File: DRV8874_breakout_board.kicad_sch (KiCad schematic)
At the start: 11 parts, among them U2 DRV8874PWPR

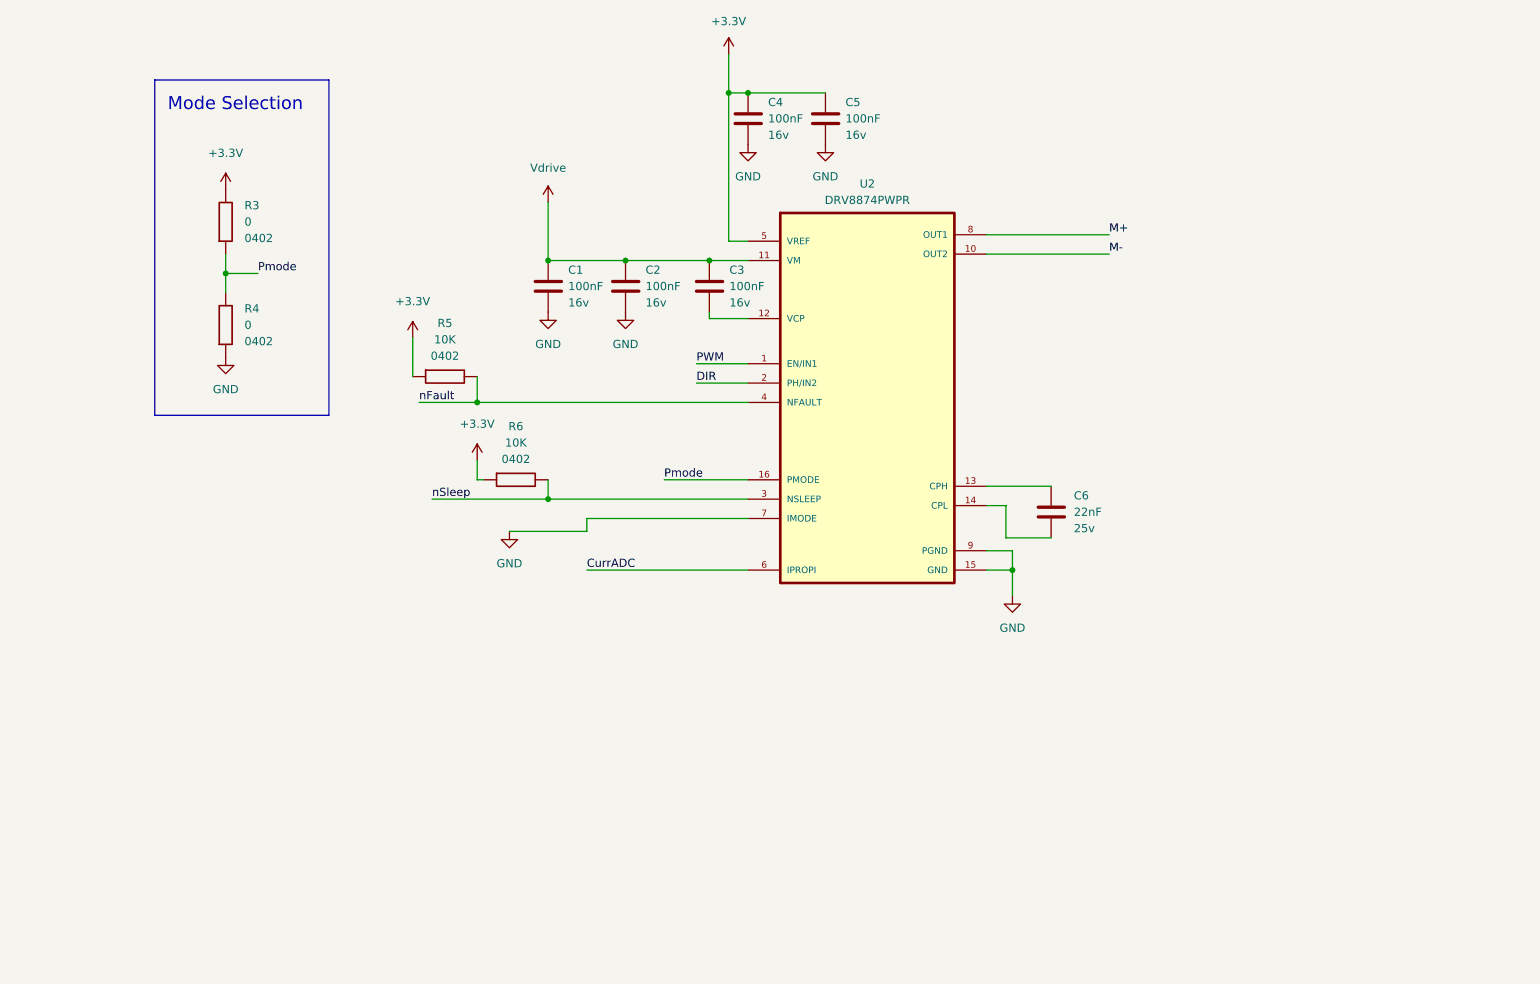
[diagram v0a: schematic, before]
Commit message: Forma de PCB con espacios para tira de pines
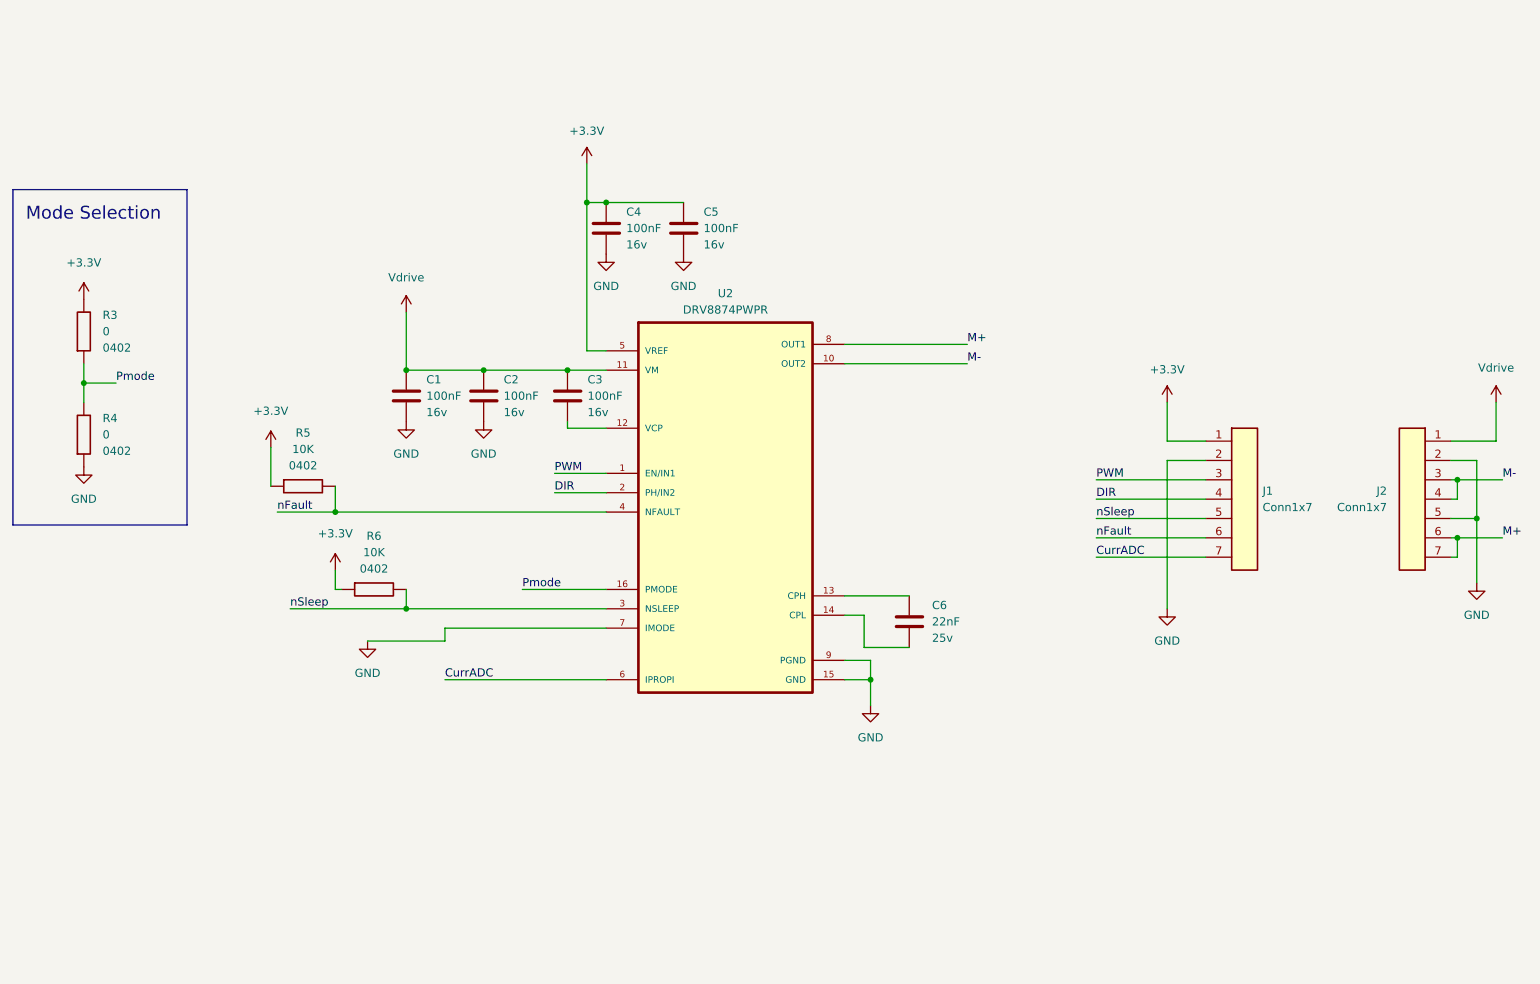
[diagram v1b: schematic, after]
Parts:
- added J1, J2: Conn1x7, Connector_PinHeader_2.54mm:PinHeader_1x07_P2.54mm_Vertical, symbol Herranz - Gen Connectors:Conn1x7
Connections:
- net +3V3: now also J1.1 (Pin_1)
- net CurrADC: now also J1.7 (Pin_7)
- net DIR: now also J1.4 (Pin_4)
- net GND: now also J1.2 (Pin_2), J2.2 (Pin_2), J2.5 (Pin_5)
- net M+: now also J2.6 (Pin_6), J2.7 (Pin_7)
- net M-: now also J2.3 (Pin_3), J2.4 (Pin_4)
- net PWM: now also J1.3 (Pin_3)
- net Vdrive: now also J2.1 (Pin_1)
- net nFault: now also J1.6 (Pin_6)
- net nSleep: now also J1.5 (Pin_5)
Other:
- moved on the sheet: C1, C2, C3, C4, C5, C6, R3, R4, R5, R6, U2

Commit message: primera iteración PCB
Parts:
- added R4: 0, Resistor_SMD:R_0402_1005Metric, symbol Herranz - Resistors (0402):0
- added R5: 62K, Resistor_SMD:R_0402_1005Metric, symbol Herranz - Resistors (0402):62K
- added U2: Logo_Small, Herranz - Various:LOGO_small, symbol Herranz - Various:Logo_Small
- R3: now not fitted
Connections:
- net CurrADC: now also R4.2
- net GND: now also R4.1, R5.1; no longer U2.7 (IMODE)
- new net: R5.2, U2.7 (IMODE)
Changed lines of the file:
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@@
   (junction (at 107 87) (diameter 0) (color 0 0 0 0)
   )
+  (junction (at 113 135) (diameter 0) (color 0 0 0 0)
+  )
   (junction (at 95 124) (diameter 0) (color 0 0 0 0)
   )
@@
     (stroke (width 0) (type default))
   )
+  (wire (pts (xy 84 129) (xy 84 127))
+    (stroke (width 0) (type default))
+  )
   (wire (pts (xy 264 98) (xy 264 92))
     (stroke (width 0) (type default))
@@
     (stroke (width 0) (type default))
   )
+  (wire (pts (xy 113 135) (xy 126 135))
+    (stroke (width 0) (type default))
+  )
   (wire (pts (xy 45 89) (xy 50 89))
     (stroke (width 0) (type default))
@@
     (stroke (width 0) (type default))
   )
-  (wire (pts (xy 89 129) (xy 101 129))
-    (stroke (width 0) (type default))
-  )
   (wire (pts (xy 257 113) (xy 258 113))
     (stroke (width 0) (type default))
@@
     (stroke (width 0) (type default))
   )
-  (wire (pts (xy 101 127) (xy 126 127))
+  (wire (pts (xy 84 127) (xy 126 127))
     (stroke (width 0) (type default))
   )
@@
     (stroke (width 0) (type default))
   )
-  (wire (pts (xy 101 135) (xy 126 135))
-    (stroke (width 0) (type default))
-  )
-  (wire (pts (xy 101 129) (xy 101 127))
+  (wire (pts (xy 101 135) (xy 113 135))
+    (stroke (width 0) (type default))
+  )
+  (wire (pts (xy 84 142) (xy 84 139))
     (stroke (width 0) (type default))
   )
@@
         (path "/a9814894-6caf-47c3-94af-538221f5e47e"
           (reference "#PWR04") (unit 1)
+        )
+      )
+    )
+  )
+  (symbol (lib_id "power:GND") (at 113 145 0) (unit 1)
+    (in_bom yes) (on_board yes) (dnp no) (fields_autoplaced)
+    (property "Reference" "#PWR0101" (at 113 151.35 0)
+      (effects (font (size 1.27 1.27)) hide)
+    )
+    (property "Value" "GND" (at 113 149.98 0)
+      (effects (font (size 1.27 1.27)))
+    )
+    (property "Footprint" "" (at 113 145 0)
+      (effects (font (size 1.27 1.27)) hide)
+    )
+    (property "Datasheet" "" (at 113 145 0)
+      (effects (font (size 1.27 1.27)) hide)
+    )
+    (pin "1")
+    (instances
+      (project "RosMechatronicBoard"
+        (path "/25a480f9-594a-4a75-8741-88ac7e0fd4ad/318900b3-2436-4284-bca8-0ffa65649c89"
+          (reference "#PWR0101") (unit 1)
+        )
+        (path "/25a480f9-594a-4a75-8741-88ac7e0fd4ad/8bbf1555-9781-4af3-bbc0-fdce319f9e3c"
+          (reference "#PWR010") (unit 1)
+        )
+        (path "/25a480f9-594a-4a75-8741-88ac7e0fd4ad/14e70d62-43dc-4725-9c42-40568e45ff10"
+          (reference "#PWR033") (unit 1)
+        )
+        (path "/25a480f9-594a-4a75-8741-88ac7e0fd4ad/d70baead-72f9-4a39-a1ce-4bdb0a4cab4d"
+          (reference "#PWR051") (unit 1)
+        )
+      )
+      (project "DRV8874_breakout_board"
+        (path "/a9814894-6caf-47c3-94af-538221f5e47e"
+          (reference "#PWR017") (unit 1)
         )
       )
@@
     )
   )
-  (symbol (lib_id "power:GND") (at 89 129 0) (unit 1)
-    (in_bom yes) (on_board yes) (dnp no) (fields_autoplaced)
-    (property "Reference" "#PWR0104" (at 89 135.35 0)
-      (effects (font (size 1.27 1.27)) hide)
-    )
-    (property "Value" "GND" (at 89 133.98 0)
-      (effects (font (size 1.27 1.27)))
-    )
-    (property "Footprint" "" (at 89 129 0)
-      (effects (font (size 1.27 1.27)) hide)
-    )
-    (property "Datasheet" "" (at 89 129 0)
+  (symbol (lib_id "power:GND") (at 84 142 0) (unit 1)
+    (in_bom yes) (on_board yes) (dnp no) (fields_autoplaced)
+    (property "Reference" "#PWR0104" (at 84 148.35 0)
+      (effects (font (size 1.27 1.27)) hide)
+    )
+    (property "Value" "GND" (at 84 146.98 0)
+      (effects (font (size 1.27 1.27)))
+    )
+    (property "Footprint" "" (at 84 142 0)
+      (effects (font (size 1.27 1.27)) hide)
+    )
+    (property "Datasheet" "" (at 84 142 0)
       (effects (font (size 1.27 1.27)) hide)
     )
@@
         (path "/a9814894-6caf-47c3-94af-538221f5e47e"
           (reference "C6") (unit 1)
+        )
+      )
+    )
+  )
+  (symbol (lib_id "Herranz - Various:Logo_Small") (at 188 178 0) (unit 1)
+    (in_bom yes) (on_board yes) (dnp no) (fields_autoplaced)
+    (property "Reference" "U2" (at 188 176 0)
+      (effects (font (size 1.27 1.27)) hide)
+    )
+    (property "Value" "Logo_Small" (at 188 181 0)
+      (effects (font (size 1.27 1.27)) hide)
+    )
+    (property "Footprint" "Herranz - Various:LOGO_small" (at 188 175 0)
+      (effects (font (size 1.27 1.27)) hide)
+    )
+    (property "Datasheet" "" (at 188 178 0)
+      (effects (font (size 1.27 1.27)) hide)
+    )
+    (instances
+      (project "DRV8874_breakout_board"
+        (path "/a9814894-6caf-47c3-94af-538221f5e47e"
+          (reference "U2") (unit 1)
         )
       )
@@
     )
   )
+  (symbol (lib_id "Herranz - Resistors (0402):62K") (at 83 134 90) (unit 1)
+    (in_bom yes) (on_board yes) (dnp no) (fields_autoplaced)
+    (property "Reference" "R5" (at 86.36 131.46 90)
+      (effects (font (size 1.27 1.27)) (justify right))
+    )
+    (property "Value" "62K" (at 86.36 134 90)
+      (effects (font (size 1.27 1.27)) (justify right))
+    )
+    (property "Footprint" "Resistor_SMD:R_0402_1005Metric" (at 80 134 0)
+      (effects (font (size 1.27 1.27)) hide)
+    )
+    (property "Datasheet" "" (at 83 134 0)
+      (effects (font (size 1.27 1.27)) hide)
+    )
+    (property "Size" "0402" (at 86.36 136.54 90)
+      (effects (font (size 1.27 1.27)) (justify right))
+    )
+    (pin "2")
+    (pin "1")
+    (instances
+      (project "DRV8874_breakout_board"
+        (path "/a9814894-6caf-47c3-94af-538221f5e47e"
+          (reference "R5") (unit 1)
+        )
+      )
+    )
+  )
   (symbol (lib_id "power:Vdrive") (at 95 78 0) (unit 1)
     (in_bom yes) (on_board yes) (dnp no) (fields_autoplaced)
@@
   )
   (symbol (lib_id "Herranz - Resistors (0402):0") (at 44 81 90) (unit 1)
-    (in_bom yes) (on_board yes) (dnp no) (fields_autoplaced)
+    (in_bom yes) (on_board yes) (dnp yes) (fields_autoplaced)
     (property "Reference" "R3" (at 47.91 78.46 90)
       (effects (font (size 1.27 1.27)) (justify right))
@@
         )
       )
+    )
+  )
+  (symbol (lib_id "Herranz - Resistors (0402):0") (at 112 140 90) (unit 1)
+    (in_bom yes) (on_board yes) (dnp no) (fields_autoplaced)
+    (property "Reference" "R4" (at 115.91 137.46 90)
+      (effects (font (size 1.27 1.27)) (justify right))
+    )
+    (property "Value" "0" (at 115.91 140 90)
+      (effects (font (size 1.27 1.27)) (justify right))
+    )
+    (property "Footprint" "Resistor_SMD:R_0402_1005Metric" (at 109 140 0)
+      (effects (font (size 1.27 1.27)) hide)
+    )
+    (property "Datasheet" "" (at 112 140 0)
+      (effects (font (size 1.27 1.27)) hide)
+    )
+    (property "Size" "0402" (at 115.91 142.54 90)
+      (effects (font (size 1.27 1.27)) (justify right))
+    )
+    (pin "1")
+    (pin "2")
+    (instances
+      (project "RosMechatronicBoard"
+        (path "/25a480f9-594a-4a75-8741-88ac7e0fd4ad/318900b3-2436-4284-bca8-0ffa65649c89"
+          (reference "R4") (unit 1)
+        )
+        (path "/25a480f9-594a-4a75-8741-88ac7e0fd4ad/8bbf1555-9781-4af3-bbc0-fdce319f9e3c"
+          (reference "R18") (unit 1)
+        )
+        (path "/25a480f9-594a-4a75-8741-88ac7e0fd4ad/14e70d62-43dc-4725-9c42-40568e45ff10"
+          (reference "R26") (unit 1)
+        )
+        (path "/25a480f9-594a-4a75-8741-88ac7e0fd4ad/d70baead-72f9-4a39-a1ce-4bdb0a4cab4d"
+          (reference "R34") (unit 1)
+        )
+      )
+      (project "DRV8874_breakout_board"
+        (path "/a9814894-6caf-47c3-94af-538221f5e47e"
+          (reference "R6") (unit 1)
+        )
+      )

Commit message: Añadido divisor de resistencia para v_ref
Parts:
- removed C4, C5: 100nF, Capacitor_SMD:C_0603_1608Metric, symbol Herranz - Capacitor (0603):Gen_C
- added C3: Gen_C, Capacitor_SMD:C_0402_1005Metric, symbol Herranz - Capacitor (0402):Gen_C
- added R6, R7: 0, Resistor_SMD:R_0402_1005Metric, symbol Herranz - Resistors (0402):0
- renumbered C1 to C?, C6 to C?, C2 to C?, C3 to C?, R5 to R4, R5 to R?, R6 to R?, R4 to R?, R3 to R?, U2 to U?
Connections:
- net +3V3: now also R6.2; no longer U?.5 (VREF)
- net GND: now also C3.2, R7.1
- new net: C3.1, R6.1, R7.2, U?.5 (VREF)

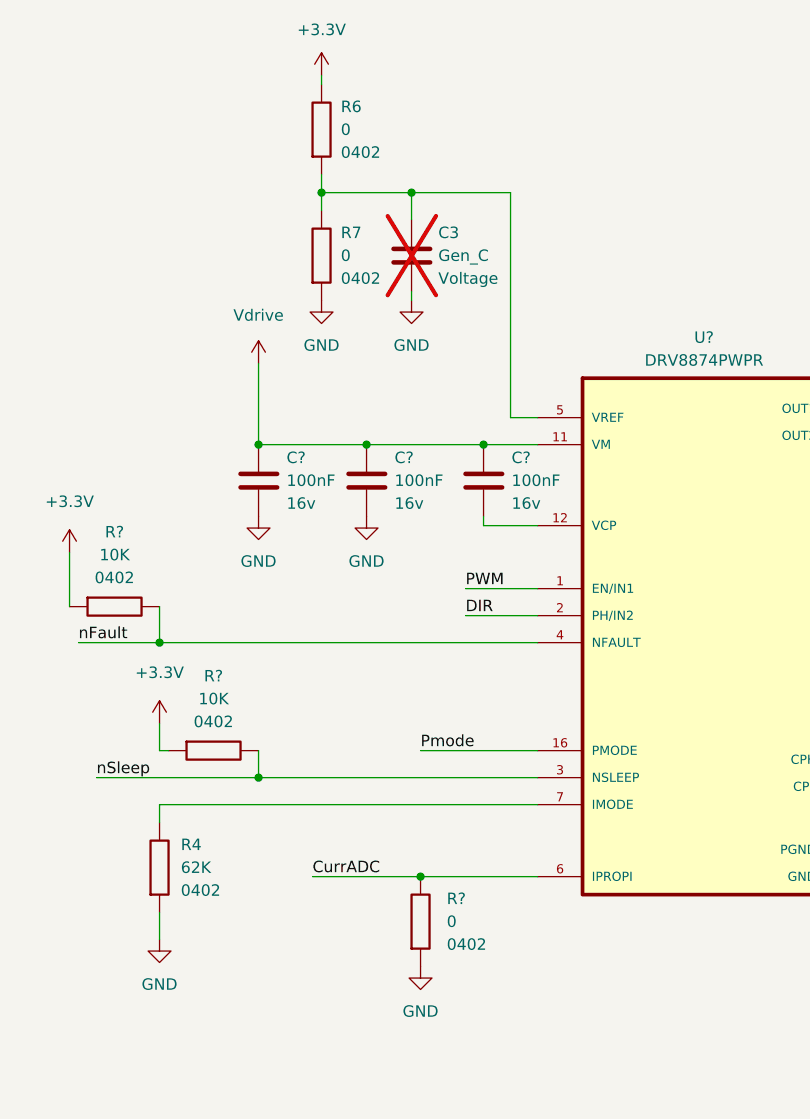
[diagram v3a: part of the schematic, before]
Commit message: añadidos LCSC y archivos de produccion
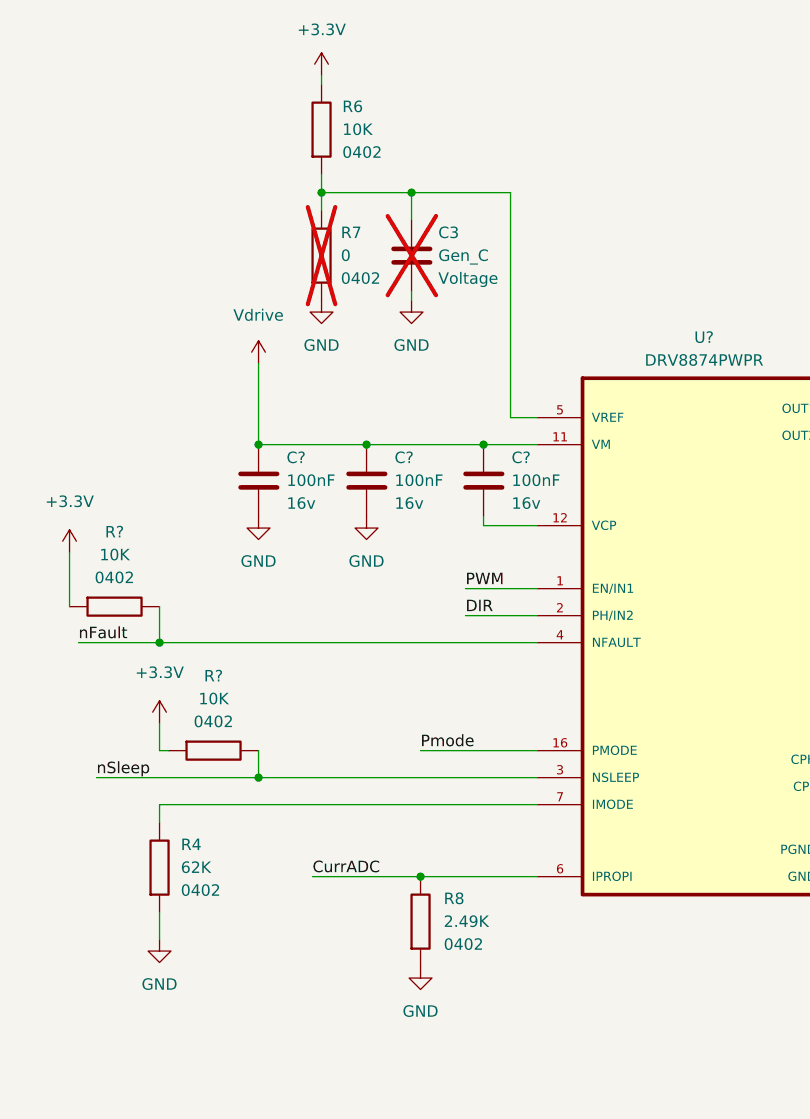
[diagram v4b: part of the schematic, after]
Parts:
- removed R6, R?: 0, Resistor_SMD:R_0402_1005Metric, symbol Herranz - Resistors (0402):0
- added R6: 10K, Resistor_SMD:R_0402_1005Metric, symbol Herranz - Resistors (0402):10K
- added R8: 2.49K, Resistor_SMD:R_0402_1005Metric, symbol Herranz - Resistors (0402):3.0K
- C? (x3): LCSC (none) -> C66501
- C?: LCSC (none) -> C779971
- R4: LCSC (none) -> C137950
- R7: now not fitted
- R? (x2): LCSC (none) -> C163478
- R? (x2): LCSC (none) -> C4044221
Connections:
- net +3V3: now also R6.2
- net CurrADC: now also R8.2
- net GND: now also R8.1
- net at C3.1, R7.2, U?.5 (VREF): now also R6.1
